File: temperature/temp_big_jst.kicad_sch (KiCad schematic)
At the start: 1 part, among them CN1 39302030

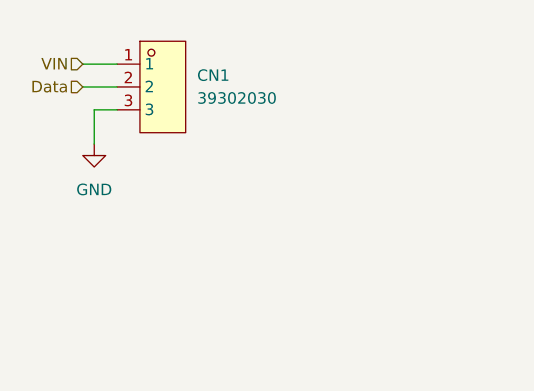
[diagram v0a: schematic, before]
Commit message: add old system temp connectors
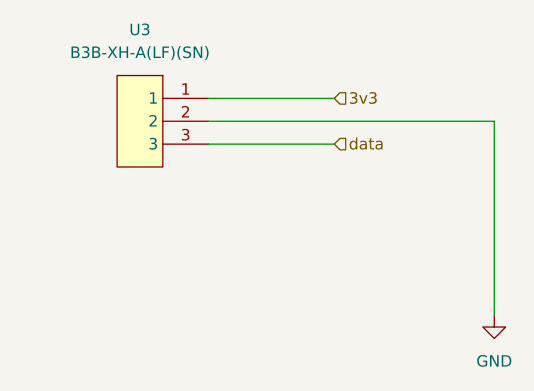
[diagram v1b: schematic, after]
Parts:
- removed CN1: 39302030, easyeda2kicad:CONN-TH_3P-P4.20_39302030, symbol easyeda2kicad:39302030
- added U3: B3B-XH-A(LF)(SN), easyeda2kicad:CONN-TH_3P-P2.50_A2501WV2-3P, symbol easyeda2kicad:B3B-XH-A(LF)(SN)
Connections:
- net GND: now also U3.2
- new net 3v3: U3.1
- new net data: U3.3
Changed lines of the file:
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@@
 	(wire
 		(pts
-			(xy 22.86 22.86) (xy 26.67 22.86)
-		)
-		(stroke
-			(width 0)
-			(type default)
-		)
-	)
-	(wire
-		(pts
-			(xy 26.67 27.94) (xy 24.13 27.94)
-		)
-		(stroke
-			(width 0)
-			(type default)
-		)
-	)
-	(wire
-		(pts
-			(xy 24.13 27.94) (xy 24.13 31.75)
-		)
-		(stroke
-			(width 0)
-			(type default)
-		)
-	)
-	(wire
-		(pts
-			(xy 22.86 25.4) (xy 26.67 25.4)
-		)
-		(stroke
-			(width 0)
-			(type default)
-		)
-	)
-	(hierarchical_label "VIN"
+			(xy 36.83 26.67) (xy 50.8 26.67)
+		)
+		(stroke
+			(width 0)
+			(type default)
+		)
+	)
+	(wire
+		(pts
+			(xy 36.83 31.75) (xy 50.8 31.75)
+		)
+		(stroke
+			(width 0)
+			(type default)
+		)
+	)
+	(wire
+		(pts
+			(xy 68.58 29.21) (xy 68.58 50.8)
+		)
+		(stroke
+			(width 0)
+			(type default)
+		)
+	)
+	(wire
+		(pts
+			(xy 36.83 29.21) (xy 68.58 29.21)
+		)
+		(stroke
+			(width 0)
+			(type default)
+		)
+	)
+	(hierarchical_label "data"
 		(shape input)
-		(at 22.86 22.86 180)
+		(at 50.8 31.75 0)
 		(effects
 			(font
 				(size 1.27 1.27)
 			)
-			(justify right)
-		)
-	)
-	(hierarchical_label "Data"
+			(justify left)
+		)
+	)
+	(hierarchical_label "3v3"
 		(shape input)
-		(at 22.86 25.4 180)
+		(at 50.8 26.67 0)
 		(effects
 			(font
 				(size 1.27 1.27)
 			)
-			(justify right)
+			(justify left)
 		)
 	)
 	(symbol
-		(lib_id "easyeda2kicad:39302030")
-		(at 31.75 25.4 0)
+		(lib_id "easyeda2kicad:B3B-XH-A(LF)(SN)")
+		(at 29.21 29.21 270)
 		(unit 1)
 		(exclude_from_sim no)
@@
 		(dnp no)
 		(fields_autoplaced yes)
-		(property "Reference" "CN1"
-			(at 35.56 24.1299 0)
-			(effects
-				(font
-					(size 1.27 1.27)
-				)
-				(justify left)
-			)
-		)
-		(property "Value" "39302030"
-			(at 35.56 26.6699 0)
-			(effects
-				(font
-					(size 1.27 1.27)
-				)
-				(justify left)
-			)
-		)
-		(property "Footprint" "easyeda2kicad:CONN-TH_3P-P4.20_39302030"
-			(at 31.75 35.56 0)
-			(effects
-				(font
-					(size 1.27 1.27)
-				)
-				(hide yes)
-			)
-		)
-		(property "Datasheet" ""
-			(at 31.75 25.4 0)
+		(property "Reference" "U3"
+			(at 29.21 19.05 90)
+			(effects
+				(font
+					(size 1.27 1.27)
+				)
+			)
+		)
+		(property "Value" "B3B-XH-A(LF)(SN)"
+			(at 29.21 21.59 90)
+			(effects
+				(font
+					(size 1.27 1.27)
+				)
+			)
+		)
+		(property "Footprint" "easyeda2kicad:CONN-TH_3P-P2.50_A2501WV2-3P"
+			(at 29.21 29.21 0)
+			(effects
+				(font
+					(size 1.27 1.27)
+				)
+				(hide yes)
+			)
+		)
+		(property "Datasheet" "https://lcsc.com/product-detail/XH-Connectors_JST-Sales-America_B3B-XH-A-LF-SN_JST-Sales-America-B3B-XH-A-LF-SN_C144394.html"
+			(at 26.67 29.21 0)
 			(effects
 				(font
@@
 		)
 		(property "Description" ""
-			(at 31.75 25.4 0)
-			(effects
-				(font
-					(size 1.27 1.27)
-				)
-				(hide yes)
-			)
-		)
-		(property "LCSC Part" "C589033"
-			(at 31.75 38.1 0)
+			(at 29.21 29.21 0)
+			(effects
+				(font
+					(size 1.27 1.27)
+				)
+				(hide yes)
+			)
+		)
+		(property "LCSC Part" "C144394"
+			(at 24.13 29.21 0)
 			(effects
 				(font
@@
 		(instances
 			(project "temperature"
-				(path "/48ddfdd8-68fa-4e63-aa18-bc113cdf8cfa/2ba6a878-ea3f-407a-a731-1195ebb443a5"
-					(reference "CN4")
-					(unit 1)
-				)
-				(path "/48ddfdd8-68fa-4e63-aa18-bc113cdf8cfa/b4bf61e5-398c-448a-aca3-15c261aa0958"
-					(reference "CN1")
-					(unit 1)
-				)
-				(path "/48ddfdd8-68fa-4e63-aa18-bc113cdf8cfa/bcc39457-9308-4c11-891d-bc9f045b8f56"
-					(reference "CN3")
-					(unit 1)
-				)
-				(path "/48ddfdd8-68fa-4e63-aa18-bc113cdf8cfa/f7612f11-672f-4d5a-8a46-5a9a7a728c48"
-					(reference "CN2")
+				(path "/48ddfdd8-68fa-4e63-aa18-bc113cdf8cfa/38af5ba2-c742-4ec1-877c-1049ae6feed0"
+					(reference "U5")
+					(unit 1)
+				)
+				(path "/48ddfdd8-68fa-4e63-aa18-bc113cdf8cfa/cccf571e-bcfd-4265-90aa-fa36d88fb6f9"
+					(reference "U4")
+					(unit 1)
+				)
+				(path "/48ddfdd8-68fa-4e63-aa18-bc113cdf8cfa/d71b7f34-41de-4e95-83a1-916916ffa06b"
+					(reference "U3")
+					(unit 1)
+				)
+				(path "/48ddfdd8-68fa-4e63-aa18-bc113cdf8cfa/dc747936-743b-44eb-92e2-c78bcadb1c44"
+					(reference "U6")
 					(unit 1)
 				)
@@
 	(symbol
 		(lib_id "power:GND")
-		(at 24.13 31.75 0)
+		(at 68.58 50.8 0)
 		(unit 1)
 		(exclude_from_sim no)
@@
 		(dnp no)
 		(fields_autoplaced yes)
-		(property "Reference" "#PWR04"
-			(at 24.13 38.1 0)
+		(property "Reference" "#PWR"
+			(at 68.58 57.15 0)
 			(effects
 				(font
@@
 		)
 		(property "Value" "GND"
-			(at 24.13 36.83 0)
+			(at 68.58 55.88 0)
 			(effects
 				(font
@@
 		)
 		(property "Footprint" ""
-			(at 24.13 31.75 0)
+			(at 68.58 50.8 0)
 			(effects
 				(font
@@
 		)
 		(property "Datasheet" ""
-			(at 24.13 31.75 0)
+			(at 68.58 50.8 0)
 			(effects
 				(font
@@
 		)
 		(property "Description" "Power symbol creates a global label with name \"GND\" , ground"
-			(at 24.13 31.75 0)
+			(at 68.58 50.8 0)
 			(effects
 				(font
@@
 		(instances
 			(project "temperature"
-				(path "/48ddfdd8-68fa-4e63-aa18-bc113cdf8cfa/2ba6a878-ea3f-407a-a731-1195ebb443a5"
-					(reference "#PWR07")
-					(unit 1)
-				)
-				(path "/48ddfdd8-68fa-4e63-aa18-bc113cdf8cfa/b4bf61e5-398c-448a-aca3-15c261aa0958"
-					(reference "#PWR04")
-					(unit 1)
-				)
-				(path "/48ddfdd8-68fa-4e63-aa18-bc113cdf8cfa/bcc39457-9308-4c11-891d-bc9f045b8f56"
-					(reference "#PWR06")
-					(unit 1)
-				)
-				(path "/48ddfdd8-68fa-4e63-aa18-bc113cdf8cfa/f7612f11-672f-4d5a-8a46-5a9a7a728c48"
-					(reference "#PWR05")
-					(unit 1)
-				)
+				(path "/48ddfdd8-68fa-4e63-aa18-bc113cdf8cfa/38af5ba2-c742-4ec1-877c-1049ae6feed0"
+					(reference "#PWR012")
+					(unit 1)
+				)
+				(path "/48ddfdd8-68fa-4e63-aa18-bc113cdf8cfa/cccf571e-bcfd-4265-90aa-fa36d88fb6f9"
+					(reference "#PWR011")
+					(unit 1)
+				)
+				(path "/48ddfdd8-68fa-4e63-aa18-bc113cdf8cfa/dc747936-743b-44eb-92e2-c78bcadb1c44"
+					(reference "#PWR013")
+					(unit 1)
+				)
